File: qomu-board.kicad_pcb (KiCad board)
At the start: 4 copper layers, 33.3 x 12.2 mm, 72 parts, among them IC1 EOS-S3, J1 FTSH-105-01-L-DV-K, J2 825437-4, J3 MC-HVT1-S02-G, J4 USB-C, Q1 RV1C002UN, Q2 RV1C002UN, Q3 RV1C002UN, SW2 Captouch Pads, U1 MIC5504-3.3YMT, U10 UHD1110-FKA, U2 MIC5504-3.3YMT, U4 GD25Q16CEIGR, U9 USB-B

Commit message: pcb: fix kicad soldermask values
These values are completely wrong for small PCBs such as Qomu. By
default, it leaves a massive gap between the soldermask and the part,
resulting in no soldermask on the part itself.

Fix the "default" value of 0.25 by setting it to 0.05, which is what
Fomu used.

Signed-off-by: Sean Cross <sean@xobs.io>
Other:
- rule pad_to_mask_clearance: 0.051 -> 0.05
- rule solder_mask_min_width: 0.25 -> 0.05
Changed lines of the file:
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@@
     (1 In1.Cu signal)
     (2 In2.Cu signal hide)
-    (31 Bottom signal hide)
+    (31 Bottom signal)
     (32 B.Adhes user hide)
     (33 F.Adhes user hide)
@@
     (36 B.SilkS user)
     (37 F.SilkS user hide)
-    (38 B.Mask user hide)
-    (39 F.Mask user hide)
+    (38 B.Mask user)
+    (39 F.Mask user)
     (40 Dwgs.User user hide)
     (41 Cmts.User user hide)
@@
     (pad_size 1 1)
     (pad_drill 0)
-    (pad_to_mask_clearance 0.051)
-    (solder_mask_min_width 0.25)
+    (pad_to_mask_clearance 0.05)
+    (solder_mask_min_width 0.05)
     (aux_axis_origin 32.8 18.1)
     (visible_elements 7FFFFF7F)

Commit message: pcb: fix soldermask pullback -- again
Kicad defaults to large soldermask pullbacks, which works fine with
large parts but creates many many solderability issues with fine-pitch
parts such as those used on Qomu. Fix this so we get an actual
soldermask on our parts.

Signed-off-by: Sean Cross <sean@xobs.io>
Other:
- rule pad_to_mask_clearance: 0.05 -> 0
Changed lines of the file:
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@@
     (pad_size 1 1)
     (pad_drill 0)
-    (pad_to_mask_clearance 0.05)
-    (solder_mask_min_width 0.05)
+    (pad_to_mask_clearance 0)
     (aux_axis_origin 32.8 18.1)
     (visible_elements 7FFFFF7F)
@@
       (drillshape 0)
       (scaleselection 1)
-      (outputdirectory "./fab/dvt1d"))
+      (outputdirectory "./fab/dvt1e"))
   )
   (net 0 "")

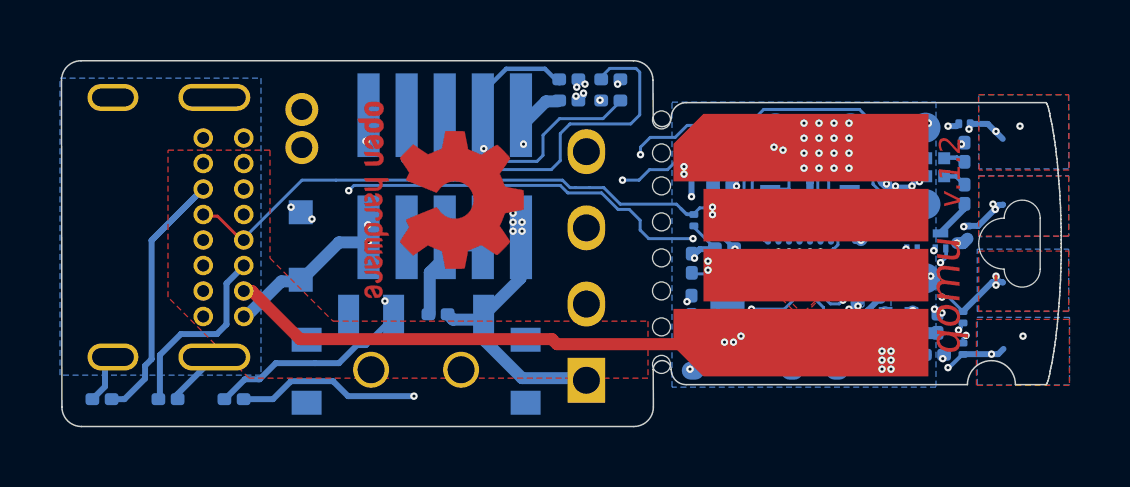
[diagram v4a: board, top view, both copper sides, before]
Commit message: pcb: add bulk caps for VDD1 and VDD2
This adds these two capacitors and keeps everything else.

Signed-off-by: Sean Cross <sean@xobs.io>
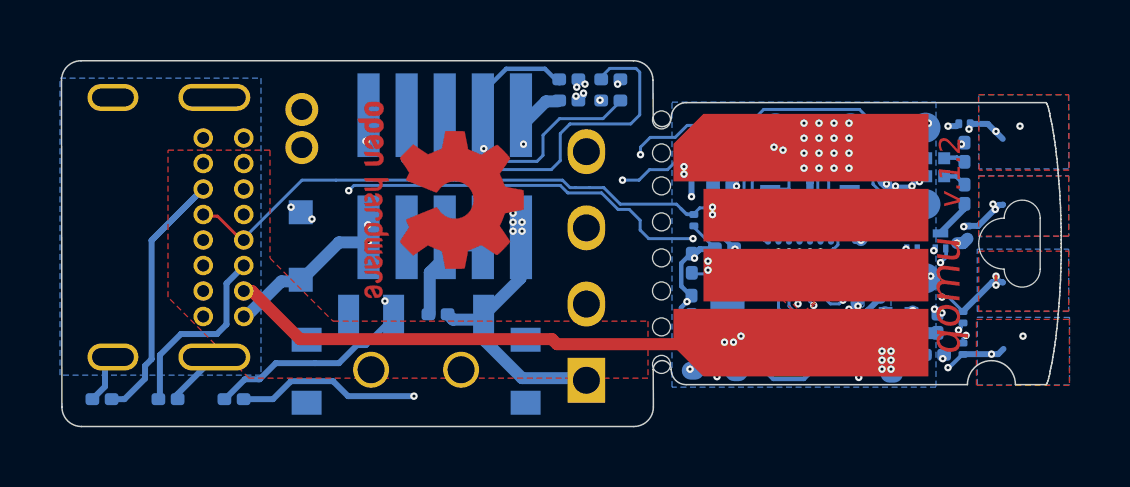
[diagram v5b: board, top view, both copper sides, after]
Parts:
- added C15: 1u, 6.3V, X5R, 0201, qomu-board-footprints:C_0201_0603Metric, B.Cu at (38.5, 25.5)
- added C4: 1u, 6.3V, X5R, 0201, qomu-board-footprints:C_0201_0603Metric, B.Cu at (37.1, 25.5)
- moved TP3 1.85 mm to (35.0, 27.1)
- moved TP2 1.83 mm to (40.1, 27.1)
- moved C6 0.65 mm to (37.1, 26.9)
- moved C7 0.65 mm to (38.5, 26.2)
- moved C9 0.65 mm to (37.1, 26.2)
- moved R2 0.65 mm to (38.5, 26.9)
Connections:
- IC1 pad A2: (no net) -> /VDD1
- IC1 pad A3: (no net) -> /VDD2
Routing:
- net GND: track 160.8 -> 165.9 mm, vias 83 -> 84
- net /SWD_IO: track 22.1 -> 24.9 mm
- net /C1: track 30.8 -> 28.4 mm
- net /VDD2: track 0.00 -> 2.16 mm
- net +3V3: track 85.9 -> 84.6 mm, vias 42 -> 41
- net /VDD1: track 0.00 -> 1.16 mm
- net /VCCIOB: track 5.72 -> 6.52 mm
- net Net-(IC1-PadA5): track 2.39 -> 2.95 mm

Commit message: pcb: add reset circuit to PCB
Signed-off-by: Sean Cross <sean@xobs.io>
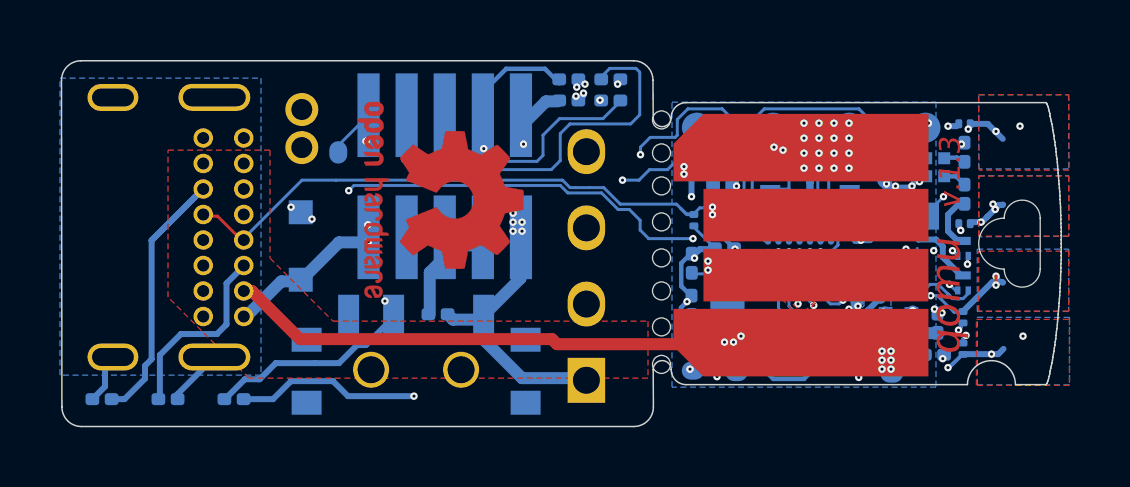
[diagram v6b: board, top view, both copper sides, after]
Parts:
- added U3: NCP803, qomu-board-footprints:SC-70_SOT-323, B.Cu at (40.7, 22.9)
- TP1: footprint qomu-board-footprints:Testpoint_pad_1mm -> qomu-board-footprints:Testpoint_smd_0_75_0_6mm
- moved TP1 20.1 mm to (21.6, 19.8), turned to 90 degrees
- moved TP6 8.04 mm to (33.6, 18.9)
- moved Q2 2.20 mm to (42.5, 24.2)
- moved Q1 0.79 mm to (42.5, 23.1)
- moved D3 0.29 mm to (42.5, 22.1), turned to 180 degrees
- moved TP7 0.08 mm to (36.2, 18.9)
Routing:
- net /SPI_SCLK: track 6.80 -> 12.1 mm, vias 2 -> 4
- net GND: track 165.9 -> 170.5 mm, vias 84 -> 86
- net Net-(Q2-Pad3): track 3.77 -> 6.59 mm
- net /VCCIOB: track 6.52 -> 8.89 mm
- net /LED_G: track 4.27 -> 6.39 mm
- net /RST_N: track 36.7 -> 35.6 mm
- net /TOUCH_3: track 8.20 -> 8.94 mm
- net /UART_TX: track 26.0 -> 26.7 mm
- net /UART_RX: track 20.4 -> 19.8 mm
- net Net-(Q1-Pad3): track 1.26 -> 1.89 mm
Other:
- board text added: "v.1.3"
- board text removed: "v.1.2"
